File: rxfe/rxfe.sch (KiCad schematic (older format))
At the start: 49 parts

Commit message: added control lines to rxfe
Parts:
- added D?: LED, symbol LED
- added P?: CONN_10, symbol CONN_10
- added R?: 1k, symbol R
- added U? (x6): 74HC04, symbol 74HC04
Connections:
- net labels added: AMP1, AMP2, VCC
- wire segments 143 -> 170

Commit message: layout of rxfe
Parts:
- added C? (x2): 100 pF, symbol C
- added C? (x2): 100 nF, symbol C
- added C?: 22 uF, symbol C
- added R? (x4): DNP, symbol R
- added R? (x2): 0, symbol R
- C? (x2): value 20 nH -> 20 nF
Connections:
- net labels added: AMP1CTL, AMP2CTL, ~AMP1, ~AMP2
- wire segments 170 -> 191
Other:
- moved on the sheet: C?, J?, L?, R?, U?, U?E, U?F

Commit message: finished layout of rx front end
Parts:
- removed D? (x4): DIODE, symbol DIODE
- added C27, C28: 20 nF, symbol C
- added P2: CONN_2, symbol CONN_2
- added U10, U11, U12: SMP1330-005LF, symbol SMP1330-005LF
- C3: renamed from C?; value C -> 20 nF
- gave numbers to parts that had none: 59
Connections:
- wire segments 191 -> 193
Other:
- moved on the sheet: R10, R11, R12, R13, R14, R8, U2D, U8

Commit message: unfinished agc board, added headers for usrp lfrx dio ports and pulldowns
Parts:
- removed P1: CONN_10, symbol CONN_10
- added J3: 4610X-AP1-103LF, symbol SIL10
- added P1: CONN_10X2, Connect:VASCH5x2, symbol CONN_10X2
- C1, C10, C11, C12, C13, C14, C15, C16, C17, C18, C19, C2, C20, C21, C22, C23, C24, C25, C26, C27, C28, C3, C4, C5, C9, D1, L4, L5, L6, L7, R1, R10, R11, R12, R13, R14, R2, R3, R4, R5, R6, R7, R8, R9: footprint (none) -> SMD_Packages:SM0805
- C6, C7, C8, L1, L2, L3: footprint (none) -> SMD_Packages:SM1210
- J1, J2: footprint (none) -> sma:sma
- P2: footprint (none) -> Connect:PINHEAD1-2
- U1: footprint (none) -> qfn24:qfn24
- U10, U11, U12: footprint (none) -> SMD_Packages:SOT23
- U2: footprint (none) -> SMD_Packages:TSSOP14
- U3: footprint (none) -> yy161:YY161
- U4, U5, U8, U9: footprint (none) -> SMD_Packages:SOT23_6
- U6, U7: footprint (none) -> Housings_SOT-23_SOT-143_TSOT-6:SC70-6
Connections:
- wire segments 193 -> 204
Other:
- note added: "TO LFRX, HEADER J15"

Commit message: fixed layout bugs on rxfe, changed usrp control header, added 12v->5v linear regulator
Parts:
- removed P1: CONN_10X2, Connect:VASCH5x2, symbol CONN_10X2
- added C29: 100 nF, SMD_Packages:SMD-0805, symbol C
- added C30: 1 uF, SMD_Packages:SMD-0805, symbol C
- added P1: CONN_8X2, Connect:VASCH10x2, symbol CONN_8X2
- added U13: LM7805, Housings_SOT-89:SOT89-3_Housing, symbol LM7805
- J3: footprint (none) -> Connect:SIL-10
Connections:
- wire segments 204 -> 218
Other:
- note added: "TO LFRX"
- note removed: "TO LFRX, HEADER J15"
- moved on the sheet: P2

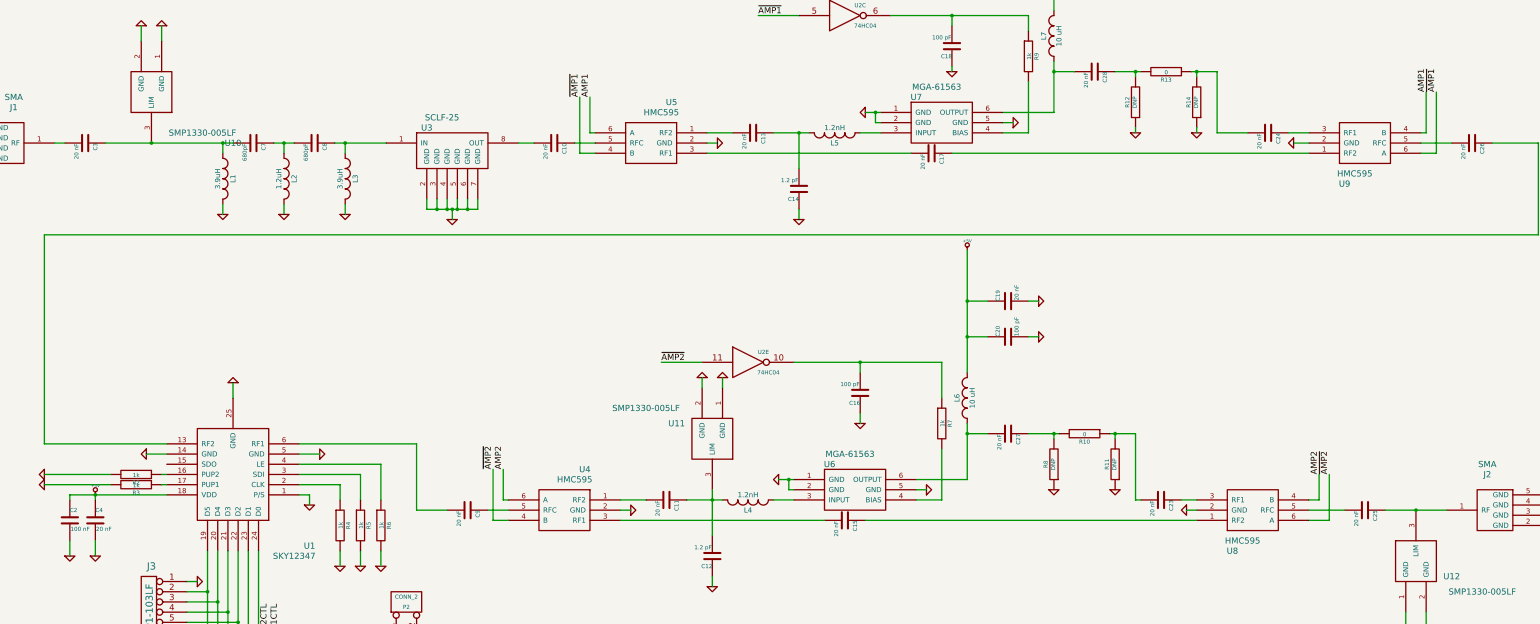
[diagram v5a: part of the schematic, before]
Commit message: added power distribution board, changed SMA connectors to top through hole, moved mounting holes on rxfe
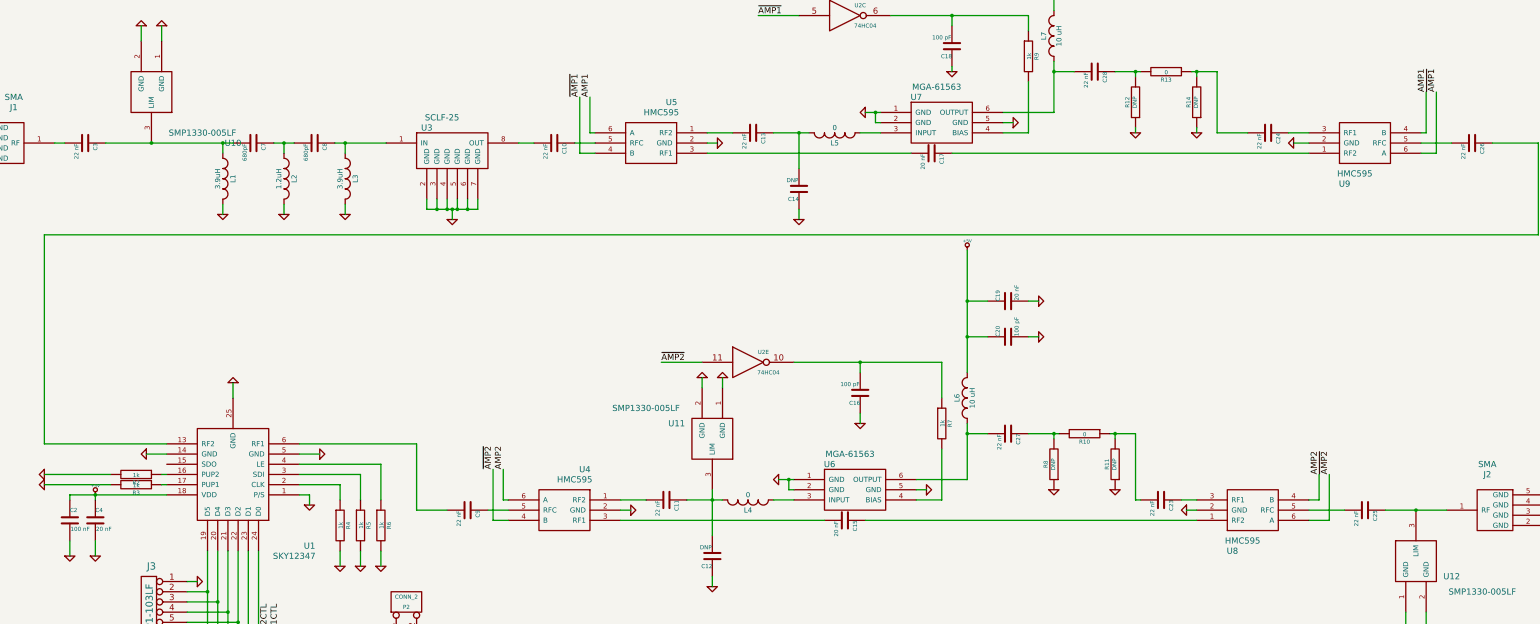
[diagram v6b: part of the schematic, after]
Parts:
- C10, C11, C13, C23, C24, C25, C26, C27, C28, C3, C9: value 20 nF -> 22 nF
- C12, C14: value 1.2 pF -> DNP
- L4, L5: value 1.2nH -> 0
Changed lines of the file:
@@
 P 2100 4000
 F 0 "C3" H 2100 4100 40  0000 L CNN
-F 1 "20 nF" H 2106 3915 40  0000 L CNN
+F 1 "22 nF" H 2106 3915 40  0000 L CNN
 F 2 "SMD_Packages:SM0805" H 2138 3850 30  0001 C CNN
 F 3 "" H 2100 4000 60  0000 C CNN
@@
 P 6700 4000
 F 0 "C10" H 6700 4100 40  0000 L CNN
-F 1 "20 nF" H 6706 3915 40  0000 L CNN
+F 1 "22 nF" H 6706 3915 40  0000 L CNN
 F 2 "SMD_Packages:SM0805" H 6738 3850 30  0001 C CNN
 F 3 "" H 6700 4000 60  0000 C CNN
@@
 P 15700 4000
 F 0 "C26" H 15700 4100 40  0000 L CNN
-F 1 "20 nF" H 15706 3915 40  0000 L CNN
+F 1 "22 nF" H 15706 3915 40  0000 L CNN
 F 2 "SMD_Packages:SM0805" H 15738 3850 30  0001 C CNN
 F 3 "" H 15700 4000 60  0000 C CNN
@@
 P 8650 3900
 F 0 "C13" H 8650 4000 40  0000 L CNN
-F 1 "20 nF" H 8656 3815 40  0000 L CNN
+F 1 "22 nF" H 8656 3815 40  0000 L CNN
 F 2 "SMD_Packages:SM0805" H 8688 3750 30  0001 C CNN
 F 3 "" H 8650 3900 60  0000 C CNN
@@
 P 13700 3900
 F 0 "C24" H 13700 4000 40  0000 L CNN
-F 1 "20 nF" H 13706 3815 40  0000 L CNN
+F 1 "22 nF" H 13706 3815 40  0000 L CNN
 F 2 "SMD_Packages:SM0805" H 13738 3750 30  0001 C CNN
 F 3 "" H 13700 3900 60  0000 C CNN
@@
 P 9100 4450
 F 0 "C14" H 9100 4550 40  0000 L CNN
-F 1 "1.2 pF" H 9106 4365 40  0000 L CNN
+F 1 "DNP" H 9106 4365 40  0000 L CNN
 F 2 "SMD_Packages:SM0805" H 9138 4300 30  0001 C CNN
 F 3 "" H 9100 4450 60  0000 C CNN
@@
 P 9450 3900
 F 0 "L5" H 9450 4000 50  0000 C CNN
-F 1 "1.2nH" H 9450 3850 50  0000 C CNN
+F 1 "0" H 9450 3850 50  0000 C CNN
 F 2 "SMD_Packages:SM0805" H 9450 3900 60  0001 C CNN
 F 3 "" H 9450 3900 60  0000 C CNN
@@
 P 5850 7600
 F 0 "C9" H 5850 7700 40  0000 L CNN
-F 1 "20 nF" H 5856 7515 40  0000 L CNN
+F 1 "22 nF" H 5856 7515 40  0000 L CNN
 F 2 "SMD_Packages:SM0805" H 5888 7450 30  0001 C CNN
 F 3 "" H 5850 7600 60  0000 C CNN
@@
 P 14650 7600
 F 0 "C25" H 14650 7700 40  0000 L CNN
-F 1 "20 nF" H 14656 7515 40  0000 L CNN
+F 1 "22 nF" H 14656 7515 40  0000 L CNN
 F 2 "SMD_Packages:SM0805" H 14688 7450 30  0001 C CNN
 F 3 "" H 14650 7600 60  0000 C CNN
@@
 P 7800 7500
 F 0 "C11" H 7800 7600 40  0000 L CNN
-F 1 "20 nF" H 7806 7415 40  0000 L CNN
+F 1 "22 nF" H 7806 7415 40  0000 L CNN
 F 2 "SMD_Packages:SM0805" H 7838 7350 30  0001 C CNN
 F 3 "" H 7800 7500 60  0000 C CNN
@@
 P 12650 7500
 F 0 "C23" H 12650 7600 40  0000 L CNN
-F 1 "20 nF" H 12656 7415 40  0000 L CNN
+F 1 "22 nF" H 12656 7415 40  0000 L CNN
 F 2 "SMD_Packages:SM0805" H 12688 7350 30  0001 C CNN
 F 3 "" H 12650 7500 60  0000 C CNN
@@
 P 8250 8050
 F 0 "C12" H 8250 8150 40  0000 L CNN
-F 1 "1.2 pF" H 8256 7965 40  0000 L CNN
+F 1 "DNP" H 8256 7965 40  0000 L CNN
 F 2 "SMD_Packages:SM0805" H 8288 7900 30  0001 C CNN
 F 3 "" H 8250 8050 60  0000 C CNN
@@
 P 8600 7500
 F 0 "L4" H 8600 7600 50  0000 C CNN
-F 1 "1.2nH" H 8600 7450 50  0000 C CNN
+F 1 "0" H 8600 7450 50  0000 C CNN
 F 2 "SMD_Packages:SM0805" H 8600 7500 60  0001 C CNN
 F 3 "" H 8600 7500 60  0000 C CNN
@@
 P 12000 3300
 F 0 "C28" H 12000 3400 40  0000 L CNN
-F 1 "20 nF" H 12006 3215 40  0000 L CNN
+F 1 "22 nF" H 12006 3215 40  0000 L CNN
 F 2 "SMD_Packages:SM0805" H 12038 3150 30  0001 C CNN
 F 3 "" H 12000 3300 60  0000 C CNN
@@
 P 11150 6850
 F 0 "C27" H 11150 6950 40  0000 L CNN
-F 1 "20 nF" H 11156 6765 40  0000 L CNN
+F 1 "22 nF" H 11156 6765 40  0000 L CNN
 F 2 "SMD_Packages:SM0805" H 11188 6700 30  0001 C CNN
 F 3 "" H 11150 6850 60  0000 C CNN

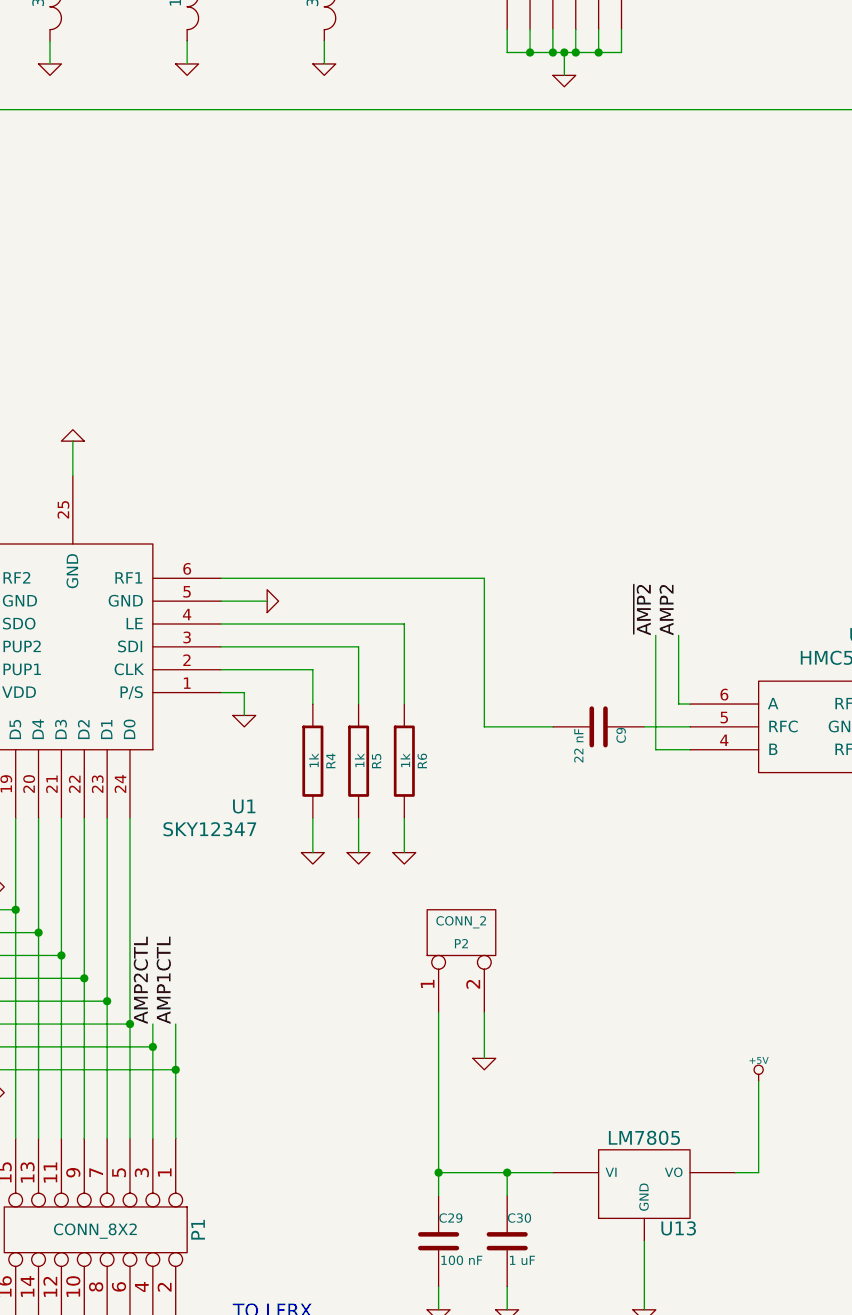
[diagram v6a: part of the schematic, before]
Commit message: added power on reset PMIC to LE on RXFE attenuator
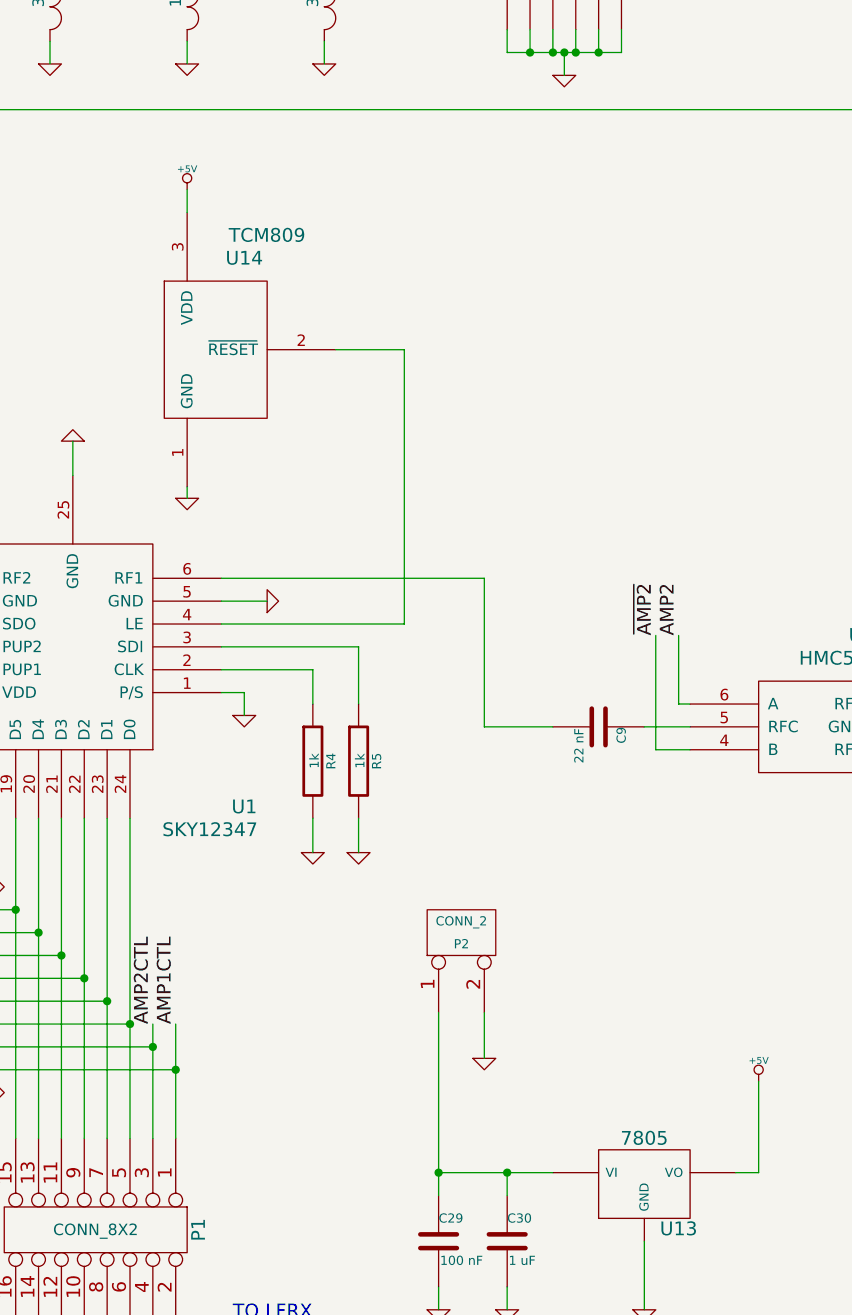
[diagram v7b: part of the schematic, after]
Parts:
- removed R6: 1k, SMD_Packages:SM0805, symbol R
- removed U13: LM7805, Housings_SOT-89:SOT89-3_Housing, symbol LM7805
- added U13: 7805, symbol 7805
- added U14: TCM809, symbol TCM809
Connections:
- net +5V: now also U13.VO, U14.3 (VDD)
- net GND: now also U13.GND, U14.1 (GND)
- net at U1.4 (LE): now also U14.2 (~RESET)
- net at C29.1, C30.1, P2.1 (P1): now also U13.VI

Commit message: moved amp from control board to rxfe
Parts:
- added C? (x2): 100 pF, SMD_Packages:SM0805, symbol C
- added C?: 20 nF, SMD_Packages:SM0805, symbol C
- added C? (x2): 22 nF, SMD_Packages:SM0805, symbol C
- added H? (x4): MOUNTING_HOLE, symbol MOUNTING_HOLE
- added L?: 10 uH, SMD_Packages:SM0805, symbol INDUCTOR_SMALL
- added R?: 1k, SMD_Packages:SM0805, symbol R
- added R?: DNP, SMD_Packages:SM0805, symbol R
- added U?: MGA-61563, Housings_SOT-23_SOT-143_TSOT-6:SC70-6, symbol MGA-61563
- added U?: SMP1330-005LF, SMD_Packages:SOT23, symbol SMP1330-005LF
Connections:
- net +5V: now also C?.1, C?.1, C?.2, L?.2, R?.1
- net GND: now also C?.1, C?.2, C?.2, U?.1 (GND), U?.1 (GND), U?.2 (GND), U?.2 (GND), U?.5 (GND)
- net at C3.1, U10.3 (LIM): now also C?.2, R?.1; no longer C7.2, L1.1
- new net: C7.2, C?.1, L1.1, R?.2, U?.3 (LIM)
- new net: C?.1, U?.3 (INPUT)
- new net: R?.2, U?.4 (BIAS)
- new net: C?.2, L?.1, U?.6 (OUTPUT)
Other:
- note added: "jumper to bypass first stage amp"
- moved on the sheet: C3, J1, U10, U2A, U2B, U2D, U2F
